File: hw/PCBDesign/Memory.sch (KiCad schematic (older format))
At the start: 12 parts, among them U4 AT25SF081, U5 AT24C256

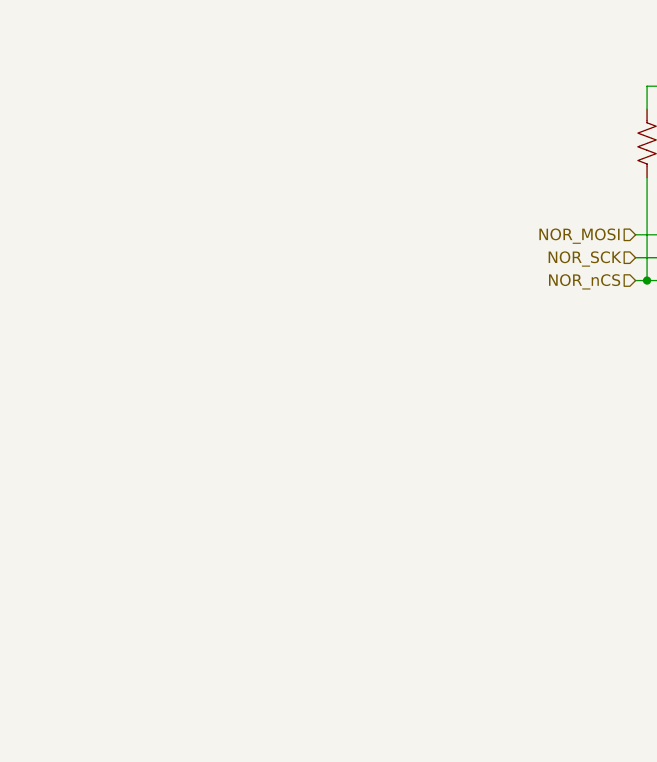
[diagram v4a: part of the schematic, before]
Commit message: Finished preliminary route of PCB after design review checklist
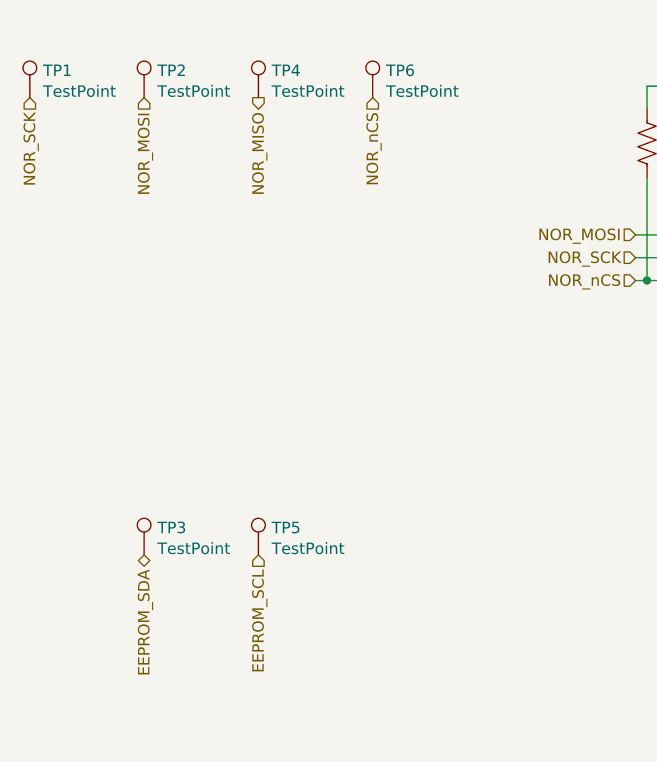
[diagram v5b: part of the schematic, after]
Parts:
- added TP1, TP2, TP3, TP4, TP5, TP6: TestPoint, TestPoint:TestPoint_Pad_2.5x2.5mm, symbol Connector:TestPoint
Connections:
- net EEPROM_SCL: now also TP5.1
- net EEPROM_SDA: now also TP3.1
- net NOR_MISO: now also TP4.1
- net NOR_MOSI: now also TP2.1
- net NOR_SCK: now also TP1.1
- net NOR_nCS: now also TP6.1
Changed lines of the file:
@@
 Wire Wire Line
 	4900 4300 5550 4300
+$Comp
+L Connector:TestPoint TP2
+U 1 1 605C449A
+P 2500 2000
+F 0 "TP2" H 2558 2118 50  0000 L CNN
+F 1 "TestPoint" H 2558 2027 50  0000 L CNN
+F 2 "TestPoint:TestPoint_Pad_2.5x2.5mm" H 2700 2000 50  0001 C CNN
+F 3 "~" H 2700 2000 50  0001 C CNN
+	1    2500 2000
+	1    0    0    -1
+$EndComp
+$Comp
+L Connector:TestPoint TP4
+U 1 1 605C46E9
+P 3000 2000
+F 0 "TP4" H 3058 2118 50  0000 L CNN
+F 1 "TestPoint" H 3058 2027 50  0000 L CNN
+F 2 "TestPoint:TestPoint_Pad_2.5x2.5mm" H 3200 2000 50  0001 C CNN
+F 3 "~" H 3200 2000 50  0001 C CNN
+	1    3000 2000
+	1    0    0    -1
+$EndComp
+$Comp
+L Connector:TestPoint TP6
+U 1 1 605C4942
+P 3500 2000
+F 0 "TP6" H 3558 2118 50  0000 L CNN
+F 1 "TestPoint" H 3558 2027 50  0000 L CNN
+F 2 "TestPoint:TestPoint_Pad_2.5x2.5mm" H 3700 2000 50  0001 C CNN
+F 3 "~" H 3700 2000 50  0001 C CNN
+	1    3500 2000
+	1    0    0    -1
+$EndComp
+$Comp
+L Connector:TestPoint TP1
+U 1 1 605C4AD4
+P 2000 2000
+F 0 "TP1" H 2058 2118 50  0000 L CNN
+F 1 "TestPoint" H 2058 2027 50  0000 L CNN
+F 2 "TestPoint:TestPoint_Pad_2.5x2.5mm" H 2200 2000 50  0001 C CNN
+F 3 "~" H 2200 2000 50  0001 C CNN
+	1    2000 2000
+	1    0    0    -1
+$EndComp
+$Comp
+L Connector:TestPoint TP3
+U 1 1 605C4DEB
+P 2500 4000
+F 0 "TP3" H 2558 4118 50  0000 L CNN
+F 1 "TestPoint" H 2558 4027 50  0000 L CNN
+F 2 "TestPoint:TestPoint_Pad_2.5x2.5mm" H 2700 4000 50  0001 C CNN
+F 3 "~" H 2700 4000 50  0001 C CNN
+	1    2500 4000
+	1    0    0    -1
+$EndComp
+$Comp
+L Connector:TestPoint TP5
+U 1 1 605C5090
+P 3000 4000
+F 0 "TP5" H 3058 4118 50  0000 L CNN
+F 1 "TestPoint" H 3058 4027 50  0000 L CNN
+F 2 "TestPoint:TestPoint_Pad_2.5x2.5mm" H 3200 4000 50  0001 C CNN
+F 3 "~" H 3200 4000 50  0001 C CNN
+	1    3000 4000
+	1    0    0    -1
+$EndComp
+Text HLabel 3500 2000 3    50   Input ~ 0
+NOR_nCS
+Text HLabel 3000 2000 3    50   Output ~ 0
+NOR_MISO
+Text HLabel 2500 2000 3    50   Input ~ 0
+NOR_MOSI
+Text HLabel 2500 4000 3    50   BiDi ~ 0
+EEPROM_SDA
+Text HLabel 3000 4000 3    50   Input ~ 0
+EEPROM_SCL
+Text HLabel 2000 2000 3    50   Input ~ 0
+NOR_SCK
 $EndSCHEMATC

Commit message: Add more work on PCB v2 design
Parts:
- removed TP1, TP2, TP3, TP4, TP5, TP6: TestPoint, TestPoint:TestPoint_Pad_2.5x2.5mm, symbol Connector:TestPoint
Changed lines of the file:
@@
 Wire Wire Line
 	4900 4300 5550 4300
-$Comp
-L Connector:TestPoint TP2
-U 1 1 605C449A
-P 2500 2000
-F 0 "TP2" H 2558 2118 50  0000 L CNN
-F 1 "TestPoint" H 2558 2027 50  0000 L CNN
-F 2 "TestPoint:TestPoint_Pad_2.5x2.5mm" H 2700 2000 50  0001 C CNN
-F 3 "~" H 2700 2000 50  0001 C CNN
-	1    2500 2000
-	1    0    0    -1
-$EndComp
-$Comp
-L Connector:TestPoint TP4
-U 1 1 605C46E9
-P 3000 2000
-F 0 "TP4" H 3058 2118 50  0000 L CNN
-F 1 "TestPoint" H 3058 2027 50  0000 L CNN
-F 2 "TestPoint:TestPoint_Pad_2.5x2.5mm" H 3200 2000 50  0001 C CNN
-F 3 "~" H 3200 2000 50  0001 C CNN
-	1    3000 2000
-	1    0    0    -1
-$EndComp
-$Comp
-L Connector:TestPoint TP6
-U 1 1 605C4942
-P 3500 2000
-F 0 "TP6" H 3558 2118 50  0000 L CNN
-F 1 "TestPoint" H 3558 2027 50  0000 L CNN
-F 2 "TestPoint:TestPoint_Pad_2.5x2.5mm" H 3700 2000 50  0001 C CNN
-F 3 "~" H 3700 2000 50  0001 C CNN
-	1    3500 2000
-	1    0    0    -1
-$EndComp
-$Comp
-L Connector:TestPoint TP1
-U 1 1 605C4AD4
-P 2000 2000
-F 0 "TP1" H 2058 2118 50  0000 L CNN
-F 1 "TestPoint" H 2058 2027 50  0000 L CNN
-F 2 "TestPoint:TestPoint_Pad_2.5x2.5mm" H 2200 2000 50  0001 C CNN
-F 3 "~" H 2200 2000 50  0001 C CNN
-	1    2000 2000
-	1    0    0    -1
-$EndComp
-$Comp
-L Connector:TestPoint TP3
-U 1 1 605C4DEB
-P 2500 4000
-F 0 "TP3" H 2558 4118 50  0000 L CNN
-F 1 "TestPoint" H 2558 4027 50  0000 L CNN
-F 2 "TestPoint:TestPoint_Pad_2.5x2.5mm" H 2700 4000 50  0001 C CNN
-F 3 "~" H 2700 4000 50  0001 C CNN
-	1    2500 4000
-	1    0    0    -1
-$EndComp
-$Comp
-L Connector:TestPoint TP5
-U 1 1 605C5090
-P 3000 4000
-F 0 "TP5" H 3058 4118 50  0000 L CNN
-F 1 "TestPoint" H 3058 4027 50  0000 L CNN
-F 2 "TestPoint:TestPoint_Pad_2.5x2.5mm" H 3200 4000 50  0001 C CNN
-F 3 "~" H 3200 4000 50  0001 C CNN
-	1    3000 4000
-	1    0    0    -1
-$EndComp
-Text HLabel 3500 2000 3    50   Input ~ 0
-NOR_nCS
-Text HLabel 3000 2000 3    50   Output ~ 0
-NOR_MISO
-Text HLabel 2500 2000 3    50   Input ~ 0
-NOR_MOSI
-Text HLabel 2500 4000 3    50   BiDi ~ 0
-EEPROM_SDA
-Text HLabel 3000 4000 3    50   Input ~ 0
-EEPROM_SCL
-Text HLabel 2000 2000 3    50   Input ~ 0
-NOR_SCK
 $EndSCHEMATC
